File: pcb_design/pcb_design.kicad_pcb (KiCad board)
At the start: 2 copper layers, 100 x 24 mm, 4 parts, among them SW1 SW_Push, SW2 SW_Push, SW3 SW_Push, U1 MOUDLE-SEEEDUINO-XIAO

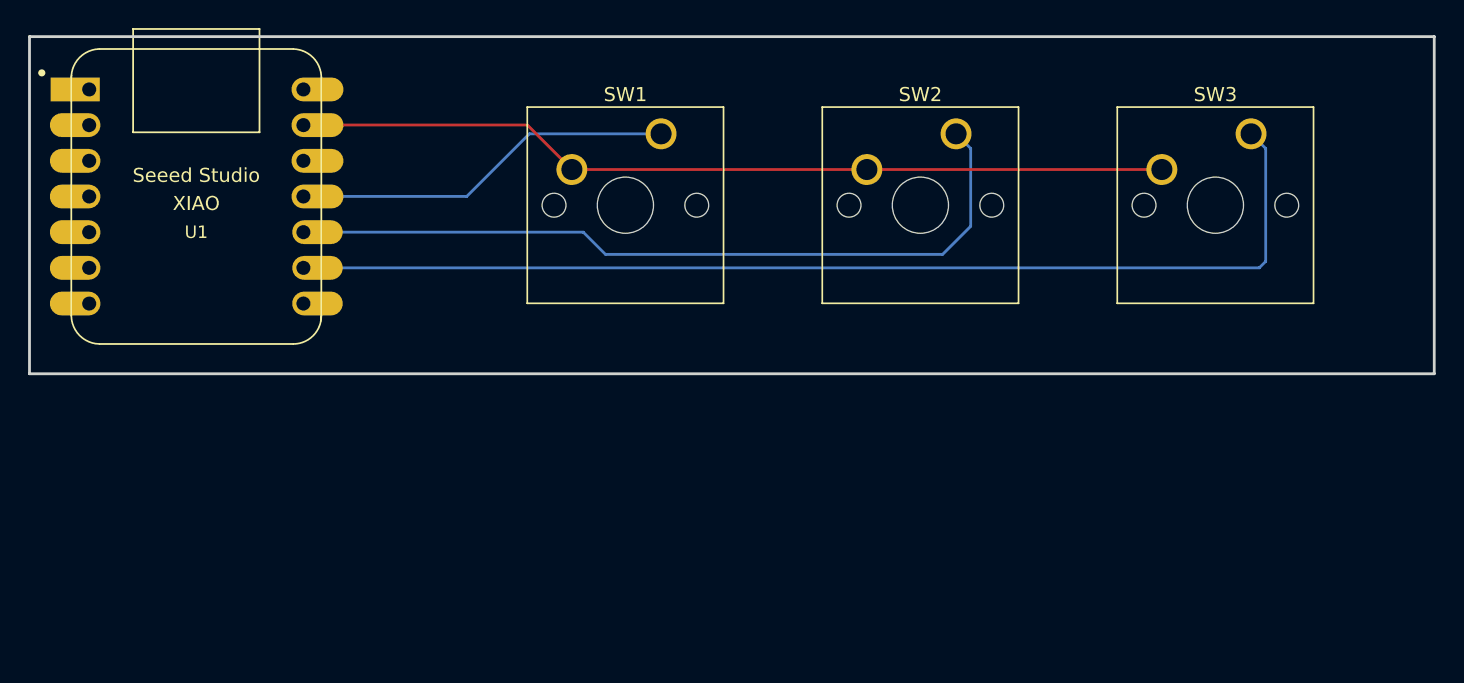
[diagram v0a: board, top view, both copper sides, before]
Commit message: Finalized PCB Design.
1st Design Iteration - Followed the guide closely to understand the usage of KiCad.
2nd Design Iteration - Discovered the DRC function which let me fix some issues with the PCB Design
3rd Design Iteration - Redesigned the PCB to my own dimensions with a unique layout.
4th Design Iteration - Added an OLED Display to the hackpad and tested with encoder, but figured it wasn't serving a key role in my planned use case.
5th Design Iteration - Redesign the PCB to the newly discovered hackclub rules.
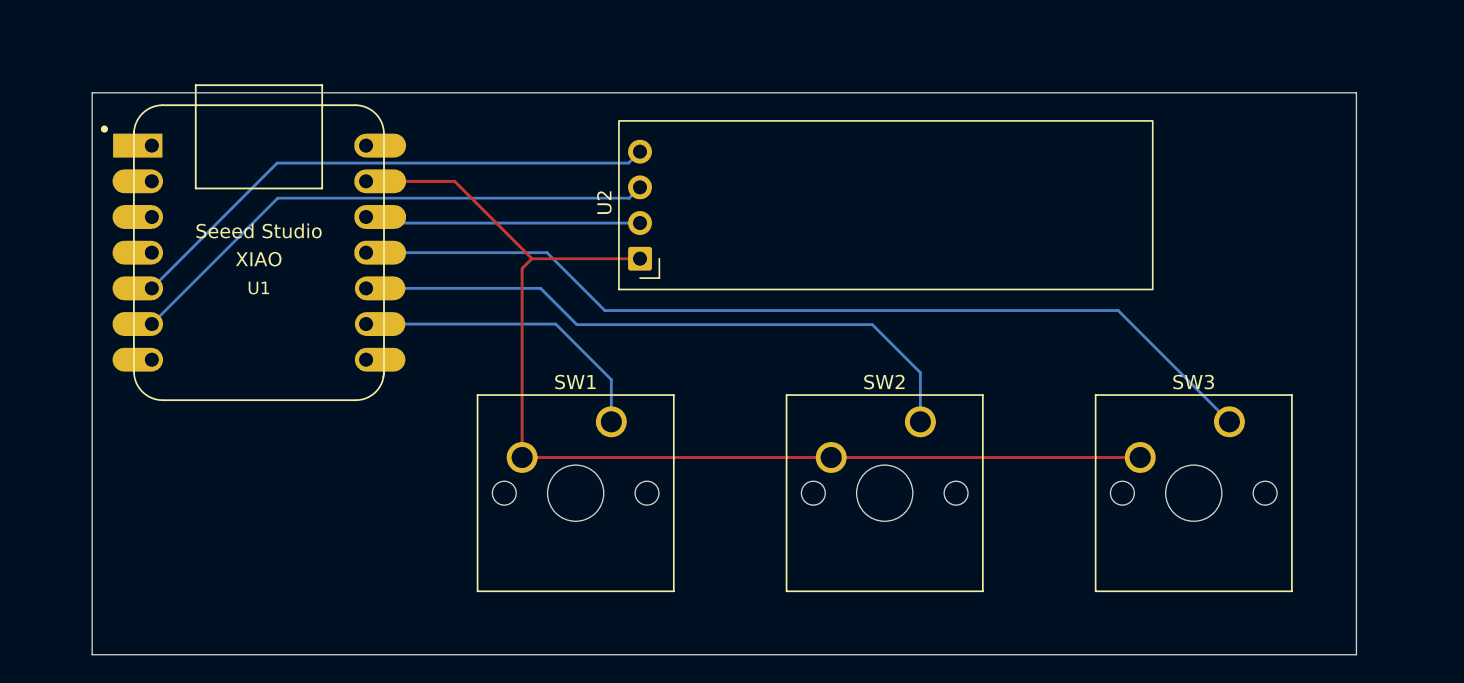
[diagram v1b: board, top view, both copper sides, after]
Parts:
- added U2: ER_OLEDM0.91_1x-I2C, Display:ER_OLEDM0.91_1x-I2C, F.Cu at (150.5, 97.8)
- moved SW1 20.8 mm to (148.4, 109.4)
- moved SW2 20.7 mm to (170.4, 109.4)
- moved SW3 20.6 mm to (192.4, 109.4)
- moved U1 5.99 mm to (123.3, 97.4)
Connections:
- SW1 pad 1: Net-(U1-PA6_A10_D10_MOSI) -> Net-(U1-PA7_A8_D8_SCK)
- SW3 pad 1: Net-(U1-PA7_A8_D8_SCK) -> Net-(U1-PA6_A10_D10_MOSI)
- U1 pad 12: unconnected-(U1-3V3-Pad12) -> Net-(U1-3V3)
- U1 pad 5: unconnected-(U1-PA8_A4_D4_SDA-Pad5) -> Net-(U1-PA8_A4_D4_SDA)
- U1 pad 6: unconnected-(U1-PA9_A5_D5_SCL-Pad6) -> Net-(U1-PA9_A5_D5_SCL)
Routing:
- net Net-(U1-PA7_A8_D8_SCK): track 78.2 -> 22.1 mm
- net Net-(U1-PA6_A10_D10_MOSI): track 27.3 -> 66.4 mm
- net Net-(U1-PA8_A4_D4_SDA): track 0.00 -> 38.8 mm
- net Net-(U1-PA9_A5_D5_SCL): track 0.00 -> 38.8 mm
- net Net-(U1-3V3): track 0.00 -> 19.7 mm
- net GND: track 62.4 -> 80.2 mm
- net Net-(U1-PA5_A9_D9_MISO): track 56.0 -> 45.4 mm
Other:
- board size 100 x 24 mm -> 90 x 40 mm
